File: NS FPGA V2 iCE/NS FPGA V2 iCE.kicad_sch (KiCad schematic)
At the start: 0 parts

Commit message: drew 30% of the schematic
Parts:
- added C1, C2, C3, C4, C5, C6, C7, C8: 10uF, symbol Device:C
- added C10, C11, C14: 0.1uF, symbol Device:C
- added C12, C13, C9: 4.7uF, symbol Device:C
- added D1: D_Schottky, symbol Device:D_Schottky
- added D2: LED, symbol Device:LED
- added J1: USB_C_Receptacle_USB2.0_14P, symbol Connector:USB_C_Receptacle_USB2.0_14P
- added R1: 1k, symbol Device:R
- added R2, R3: 5.1k, symbol Device:R
- added R4: 47.5k, symbol Device:R
- added R5: 22.1k, symbol Device:R
- added R6: 10k, symbol Device:R
- added U1: ICE40UP5K-SG48ITR, Package_DFN_QFN:QFN-48-1EP_7x7mm_P0.5mm_EP5.1x5.1mm, symbol FPGA_Lattice:ICE40UP5K-SG48ITR
- added U2: W25Q128JVS, Package_SO:SOIC-8_5.3x5.3mm_P1.27mm, symbol Memory_Flash:W25Q128JVS
- added U3: CP2102N-Axx-xQFN24, Package_DFN_QFN:QFN-24-1EP_4x4mm_P0.5mm_EP2.6x2.6mm, symbol Interface_USB:CP2102N-Axx-xQFN24
- added U4: AP2112K-3.3, Package_TO_SOT_SMD:SOT-23-5, symbol Regulator_Linear:AP2112K-3.3
- added U5: AP2112K-1.2, Package_TO_SOT_SMD:SOT-23-5, symbol Regulator_Linear:AP2112K-1.2
- added U6: AP2112K-2.5, Package_TO_SOT_SMD:SOT-23-5, symbol Regulator_Linear:AP2112K-2.5
- added U7: AP2112K-1.8, Package_TO_SOT_SMD:SOT-23-5, symbol Regulator_Linear:AP2112K-1.8
- added Y1: SG-210STF, Oscillator:Oscillator_SMD_SeikoEpson_SG210-4Pin_2.5x2.0mm, symbol Oscillator:SG-210STF
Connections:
- new net: C1.2, U4.1 (VIN), U4.3 (EN)
- new net: C4.2, U5.5 (VOUT)
- new net: J1.A5 (CC1), R2.1
- new net: J1.B5 (CC2), R3.1
- new net: C5.2, U6.1 (VIN), U6.3 (EN)
- new net: C2.2, U4.5 (VOUT)
- new net: C7.2, U7.1 (VIN), U7.3 (EN)
- new net: C3.2, U5.1 (VIN), U5.3 (EN)
- new net: C8.2, U7.5 (VOUT)
- new net: C13.1, C14.1, R6.2, U3.5 (VIO), U3.6 (VDD)
- new net: R4.1, R5.2, U3.8 (VBUS)
- new net: R6.1, U3.9 (~{RST})
- new net: U1.30 (VCC), U1.5 (VCC)
- new net: C6.2, U6.5 (VOUT)
- new net: D2.2 (A), R1.1
- new net +1V2: C4.1
- new net +1V8: C8.1
- new net +2V5: C6.1
- new net +3V3: C2.1, C3.1, C5.1, C7.1
- new net +5V: C1.1, C10.1, C9.1, D1.2 (A), J1.A4 (VBUS), J1.A9 (VBUS), J1.B4 (VBUS), J1.B9 (VBUS), R1.2, R5.1
- new net +5VP: C11.1, C12.1, D1.1 (K), U3.7 (VREGIN)
- new net D+: J1.A6 (D+), J1.B6 (D+), U3.3 (D+)
- new net D-: J1.A7 (D-), J1.B7 (D-), U3.4 (D-)
- new net GND: C10.2, C11.2, C12.2, C13.2, C14.2, C9.2, D2.1 (K), J1.A1 (GND), J1.A12 (GND), J1.B1 (GND), J1.B12 (GND), J1.S1 (SHIELD), R2.2, R3.2, R4.2, U3.2 (GND), U3.25 (GND), U4.2 (GND), U5.2 (GND), U6.2 (GND), U7.2 (GND)
- no-connect marks 0 -> 14
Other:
- note added: "NS iCE40UP FPGA"

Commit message: worked on the chip power delivery and power initialization timing
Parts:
- added C15, C17: 100nF, symbol Device:C
- added C16: 10uF, symbol Device:C
- added J2, J3: Conn_01x20_Pin, symbol Connector:Conn_01x20_Pin
- added R7: 10k, symbol Device:R
- added R8: 100, symbol Device:R
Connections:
- net +1V2: now also U1.30 (VCC), U1.5 (VCC), R8.2
- net +1V8: now also J2.5 (Pin_5)
- net +2V5: now also U1.24 (VPP_2V5), J2.4 (Pin_4)
- net +3V3: now also J2.3 (Pin_3)
- net +5V: now also J2.1 (Pin_1)
- net +5VP: now also U5.3 (EN), C15.2, R7.1
- net GND: now also U1.49 (GND), U2.4 (GND), Y1.2 (GND), C15.1, C16.2, C17.2, J2.2 (Pin_2)
- net at C1.2, U4.1 (VIN): no longer U4.3 (EN)
- net at C3.2, U5.1 (VIN): no longer U5.3 (EN)
- net at U1.29 (VCCPLL): now also C16.1, C17.1, R8.1
- new net: R7.2, U4.3 (EN)
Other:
- note added: "0603, 5%"

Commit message: added split differential voltage input selectors for each FPGA bank, wired up OSC and fixed vreg circuitry
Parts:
- added C18, C19: 0.1uF, symbol Device:C
- added D3: LED_ARGB, symbol Device:LED_ARGB
- added J4, J5: Conn_02x03_Odd_Even, symbol Connector_Generic:Conn_02x03_Odd_Even
- added J6: Conn_01x07_Pin, symbol Connector:Conn_01x07_Pin
- added R10, R11, R15: 10k, symbol Device:R
- added R12, R13, R14: 1.5k, symbol Device:R
- added R9: R22, symbol Device:R
- added SW1: SW_Push, symbol Switch:SW_Push
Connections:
- net +1V8: now also J4.2 (Pin_2), J5.2 (Pin_2)
- net +2V5: now also J4.4 (Pin_4), J5.4 (Pin_4)
- net +3V3: now also U1.22 (SPI_VCCIO1), U2.3 (~{WP}/IO_{2}), U2.7 (~{HOLD}/~{RESET}/IO_{3}), U2.8 (VCC), Y1.4 (Vcc), C18.2, C19.2, D3.1 (A), J4.6 (Pin_6), J5.6 (Pin_6), J6.1 (Pin_1), R10.1, R11.2
- net GND: now also C18.1, C19.1, J6.2 (Pin_2), SW1.2
- net SPI_SO: now reaches U1.14 (IOB_32a_SPI_SO)
- net SPI_SO: now also U2.2 (DO/IO_{1}), J6.5 (Pin_5)
- net SPI_SCK: now reaches U1.15 (IOB_34a_SPI_SCK)
- net SPI_SCK: now also U2.6 (CLK), J6.4 (Pin_4)
- net SPI_SS: now reaches U1.16 (IOB_35b_SPI_SS)
- net SPI_SS: now also U2.1 (~{CS}), J6.3 (Pin_3), R11.1
- net SPI_SI: now reaches U1.17 (IOB_33b_SPI_SI)
- net SPI_SI: now also U2.5 (DI/IO_{0}), J6.6 (Pin_6)
- net RXD: now reaches U1.18 (IOB_31b)
- net RXD: now also U3.20 (RXD)
- net FPGA_CLK: now reaches U1.20 (IOB_25b_G3)
- net FPGA_CLK: now also R9.2
- net TXD: now reaches U1.6 (IOB_13b)
- net TXD: now also U3.21 (TXD)
- net CRESET_B: now reaches U1.8 (~{CRESET})
- net CRESET_B: now also J6.7 (Pin_7)
- net at Y1.1 (~{ST}): now also R10.2
- net at Y1.3 (OUT): now also R9.1
- net at U1.33 (VCCIO_0): now also J4.1 (Pin_1), J4.3 (Pin_3), J4.5 (Pin_5), R15.2
- net at U1.39 (RGB0): now also R12.1
- net at U1.40 (RGB1): now also R13.1
- net at U1.41 (RGB2): now also R14.1
- net at U1.42 (IOT_51a): now also R15.1, SW1.1
- net at U1.1 (VCCIO_2): now also J5.1 (Pin_1), J5.3 (Pin_3), J5.5 (Pin_5)
- new net: D3.2 (RK), R12.2
- new net: D3.3 (GK), R13.2
- new net: D3.4 (BK), R14.2
- no-connect marks 14 -> 12
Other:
- moved on the sheet: J3

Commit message: completed drawing
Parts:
- added C20, C21, C22, C23, C24, C26: 0.1uF, symbol Device:C
- added C25: 1uF, symbol Device:C
- added D4: LED, symbol Device:LED
- added R16: 10k, symbol Device:R
- added R17: 1.5k, symbol Device:R
- added TP1, TP2, TP3, TP4: TestPoint_Small, symbol Connector:TestPoint_Small
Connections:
- net +1V2: now also C20.1, C24.1, C25.1, TP3.1
- net +1V8: now also TP4.1
- net +2V5: now also C26.2, TP2.1
- net +3V3: now also J2.18 (Pin_18), J3.18 (Pin_18), C21.1, TP1.1
- net +5V: now also J3.20 (Pin_20)
- net CRESET_B: now also R16.2; no longer U1.8 (~{CRESET})
- net GND: now also J2.10 (Pin_10), J2.19 (Pin_19), J3.10 (Pin_10), J3.19 (Pin_19), J3.2 (Pin_2), C20.2, C21.2, C22.2, C23.2, C24.2, C25.2, C26.1, R17.1
- net VCCIO_2: now reaches J5.1 (Pin_1), J5.3 (Pin_3), J5.5 (Pin_5), U1.1 (VCCIO_2)
- net VCCIO_2: now also C23.1
- net 1OB_18a: now reaches U1.10 (IOB_18a)
- net IOB_20a: now reaches U1.11 (IOB_20a)
- net IOB_22a: now reaches U1.12 (IOB_22a)
- net IOB_24a: now reaches U1.13 (IOB_24a)
- net IOB_29b: now reaches U1.19 (IOB_29b)
- net IOB_23b: now reaches U1.21 (IOB_23b)
- net at U1.7 (CDONE): now also D4.2 (A)
- net IOB_12a: now reaches U1.9 (IOB_16a)
- net IOT_37a: now reaches U1.23 (IOT_37a)
- net IOT_36b: now reaches U1.25 (IOT_36b)
- net IOT_39a: now reaches U1.26 (IOT_39a)
- net IOT_38b: now reaches U1.27 (IOT_38b)
- net IOT_41a: now reaches U1.28 (IOT_41a)
- net IOT_42b: now reaches U1.31 (IOT_42b)
- net IOT_43a: now reaches U1.32 (IOT_43a)
- net VCCIO_0: now reaches J4.1 (Pin_1), J4.3 (Pin_3), J4.5 (Pin_5), R15.2, U1.33 (VCCIO_0)
- net VCCIO_0: now also C22.1
- net IOT_44b: now reaches U1.34 (IOT_44b)
- net IOT_46b_G0: now reaches U1.35 (IOT_46b_G0)
- net IOT_48b: now reaches U1.36 (IOT_48b)
- net IOT_45a_G1: now reaches U1.37 (IOT_45a_G1)
- net IOT_50b: now reaches U1.38 (IOT_50b)
- net IOT_49a: now reaches U1.43 (IOT_49a)
- net IOB_6a: now reaches U1.2 (IOB_6a)
- net IOB_9b: now reaches U1.3 (IOB_9b)
- net IOB_8a: now reaches U1.4 (IOB_8a)
- net IOB_3b_G6: now reaches U1.44 (IOB_3b_G6)
- net IOB_5b: now reaches U1.45 (IOB_5b)
- net IOB_Oa: now reaches U1.46 (IOB_0a)
- net IOB_2a: now reaches U1.47 (IOB_2a)
- net IOB_4a: now reaches U1.48 (IOB_4a)
- new net: R16.1, U1.8 (~{CRESET})
- new net: D4.1 (K), R17.2
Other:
- moved on the sheet: C18, R10, R9, Y1

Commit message: assigned footprints
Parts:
- C1, C2, C3, C4, C5, C6, C7, C8: footprint (none) -> Capacitor_SMD:C_0603_1608Metric
- C10, C11, C12, C13, C14, C15, C16, C17, C18, C19, C20, C21, C22, C23, C24, C25, C26, C9: footprint (none) -> Capacitor_SMD:C_0402_1005Metric
- D1: footprint (none) -> Diode_SMD:D_0603_1608Metric
- D2, D4: footprint (none) -> LED_SMD:LED_0402_1005Metric
- D3: footprint (none) -> LED_SMD:LED_Cree-PLCC4_5x5mm_CW
- J1: footprint (none) -> Connector_USB:USB_C_Receptacle_HRO_TYPE-C-31-M-12
- J2, J3: footprint (none) -> Connector_PinHeader_2.54mm:PinHeader_1x20_P2.54mm_Vertical
- J4, J5: footprint (none) -> Connector_IDC:IDC-Header_2x03_P2.54mm_Vertical
- J6: footprint (none) -> Connector_PinHeader_2.54mm:PinHeader_1x07_P2.54mm_Vertical
- R1, R10, R11, R12, R13, R14, R15, R16, R17, R4, R5, R6, R7, R9: footprint (none) -> Resistor_SMD:R_0402_1005Metric
- R2, R3, R8: footprint (none) -> Resistor_SMD:R_0603_1608Metric
- SW1: footprint (none) -> Button_Switch_SMD:SW_Push_1P1T_NO_CK_KMR2
- TP1, TP2, TP3, TP4: footprint (none) -> TestPoint:TestPoint_Pad_D1.0mm
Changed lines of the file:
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@@
 			)
 		)
-		(property "Footprint" ""
+		(property "Footprint" "Capacitor_SMD:C_0402_1005Metric"
 			(at 145.7452 166.37 0)
 			(effects
@@
 			)
 		)
-		(property "Footprint" ""
+		(property "Footprint" "LED_SMD:LED_Cree-PLCC4_5x5mm_CW"
 			(at 90.17 101.6 0)
 			(effects
@@
 			)
 		)
-		(property "Footprint" ""
+		(property "Footprint" "Capacitor_SMD:C_0603_1608Metric"
 			(at 136.8552 224.79 0)
 			(effects
@@
 			)
 		)
-		(property "Footprint" ""
+		(property "Footprint" "Capacitor_SMD:C_0402_1005Metric"
 			(at 269.24 103.1748 0)
 			(effects
@@
 			)
 		)
-		(property "Footprint" ""
+		(property "Footprint" "Resistor_SMD:R_0402_1005Metric"
 			(at 74.93 133.858 90)
 			(effects
@@
 			)
 		)
-		(property "Footprint" ""
+		(property "Footprint" "Connector_IDC:IDC-Header_2x03_P2.54mm_Vertical"
 			(at 90.17 212.09 0)
 			(effects
@@
 			)
 		)
-		(property "Footprint" ""
+		(property "Footprint" "Capacitor_SMD:C_0402_1005Metric"
 			(at 171.1452 69.85 0)
 			(effects
@@
 			)
 		)
-		(property "Footprint" ""
+		(property "Footprint" "Resistor_SMD:R_0402_1005Metric"
 			(at 140.97 229.108 90)
 			(effects
@@
 			)
 		)
-		(property "Footprint" ""
+		(property "Footprint" "Resistor_SMD:R_0402_1005Metric"
 			(at 34.29 133.858 90)
 			(effects
@@
 			)
 		)
-		(property "Footprint" ""
+		(property "Footprint" "Capacitor_SMD:C_0603_1608Metric"
 			(at 225.7552 224.79 0)
 			(effects
@@
 			)
 		)
-		(property "Footprint" ""
+		(property "Footprint" "Connector_USB:USB_C_Receptacle_HRO_TYPE-C-31-M-12"
 			(at 354.33 95.25 0)
 			(effects
@@
 			)
 		)
-		(property "Footprint" ""
+		(property "Footprint" "Capacitor_SMD:C_0603_1608Metric"
 			(at 136.8552 254 0)
 			(effects
@@
 			)
 		)
-		(property "Footprint" ""
+		(property "Footprint" "Capacitor_SMD:C_0603_1608Metric"
 			(at 167.3352 224.79 0)
 			(effects
@@
 			)
 		)
-		(property "Footprint" ""
+		(property "Footprint" "Capacitor_SMD:C_0603_1608Metric"
 			(at 194.0052 254 0)
 			(effects
@@
 			)
 		)
-		(property "Footprint" ""
+		(property "Footprint" "Capacitor_SMD:C_0603_1608Metric"
 			(at 224.4852 254 0)
 			(effects
@@
 			)
 		)
-		(property "Footprint" ""
+		(property "Footprint" "Capacitor_SMD:C_0402_1005Metric"
 			(at 387.35 67.6148 0)
 			(effects
@@
 			)
 		)
-		(property "Footprint" ""
+		(property "Footprint" "Connector_PinHeader_2.54mm:PinHeader_1x20_P2.54mm_Vertical"
 			(at 344.17 205.74 0)
 			(effects
@@
 			)
 		)
-		(property "Footprint" ""
+		(property "Footprint" "Resistor_SMD:R_0603_1608Metric"
 			(at 372.11 89.408 90)
 			(effects
@@
 			)
 		)
-		(property "Footprint" ""
+		(property "Footprint" "Button_Switch_SMD:SW_Push_1P1T_NO_CK_KMR2"
 			(at 90.17 72.39 0)
 			(effects
@@
 			)
 		)
-		(property "Footprint" ""
+		(property "Footprint" "Capacitor_SMD:C_0402_1005Metric"
 			(at 136.1948 227.33 0)
 			(effects
@@
 			)
 		)
-		(property "Footprint" ""
+		(property "Footprint" "Resistor_SMD:R_0402_1005Metric"
 			(at 81.28 97.028 90)
 			(effects
@@
 			)
 		)
-		(property "Footprint" ""
+		(property "Footprint" "TestPoint:TestPoint_Pad_D1.0mm"
 			(at 175.26 215.9 0)
 			(effects
@@
 			)
 		)
-		(property "Footprint" ""
+		(property "Footprint" "Resistor_SMD:R_0402_1005Metric"
 			(at 172.72 124.968 90)
 			(effects
@@
 			)
 		)
-		(property "Footprint" ""
+		(property "Footprint" "Capacitor_SMD:C_0402_1005Metric"
 			(at 129.2352 166.37 0)
 			(effects
@@
 			)
 		)
-		(property "Footprint" ""
+		(property "Footprint" "Capacitor_SMD:C_0603_1608Metric"
 			(at 167.3352 254 0)
 			(effects
@@
 			)
 		)
-		(property "Footprint" ""
+		(property "Footprint" "Capacitor_SMD:C_0402_1005Metric"
 			(at 387.35 73.9648 0)
 			(effects
@@
 			)
 		)
-		(property "Footprint" ""
+		(property "Footprint" "TestPoint:TestPoint_Pad_D1.0mm"
 			(at 237.49 214.63 0)
 			(effects
@@
 			)
 		)
-		(property "Footprint" ""
+		(property "Footprint" "Capacitor_SMD:C_0402_1005Metric"
 			(at 177.4952 166.37 0)
 			(effects
@@
 			)
 		)
-		(property "Footprint" ""
+		(property "Footprint" "Capacitor_SMD:C_0402_1005Metric"
 			(at 161.29 48.5648 0)
 			(effects
@@
 			)
 		)
-		(property "Footprint" ""
+		(property "Footprint" "Capacitor_SMD:C_0603_1608Metric"
 			(at 194.0052 224.79 0)
 			(effects
@@
 			)
 		)
-		(property "Footprint" ""
+		(property "Footprint" "Diode_SMD:D_0603_1608Metric"
 			(at 386.08 48.26 0)
 			(effects
@@
 			)
 		)
-		(property "Footprint" ""
+		(property "Footprint" "TestPoint:TestPoint_Pad_D1.0mm"
 			(at 240.03 245.11 0)
 			(effects
@@
 			)
 		)
-		(property "Footprint" ""
+		(property "Footprint" "Resistor_SMD:R_0402_1005Metric"
 			(at 195.58 124.968 90)
 			(effects
@@
 			)
 		)
-		(property "Footprint" ""
+		(property "Footprint" "Capacitor_SMD:C_0402_1005Metric"
 			(at 181.3052 69.85 0)
 			(effects
@@
 			)
 		)
-		(property "Footprint" ""
+		(property "Footprint" "LED_SMD:LED_0402_1005Metric"
 			(at 356.87 43.18 0)
 			(effects
@@
 			)
 		)
-		(property "Footprint" ""
+		(property "Footprint" "Capacitor_SMD:C_0402_1005Metric"
 			(at 187.96 112.7252 0)
 			(effects
@@
 			)
 		)
-		(property "Footprint" ""
+		(property "Footprint" "Connector_PinHeader_2.54mm:PinHeader_1x20_P2.54mm_Vertical"
 			(at 373.38 205.74 0)
 			(effects
@@
 			)
 		)
-		(property "Footprint" ""
+		(property "Footprint" "Capacitor_SMD:C_0402_1005Metric"
 			(at 161.29 42.2148 0)
 			(effects
@@
 			)
 		)
-		(property "Footprint" ""
+		(property "Footprint" "Resistor_SMD:R_0603_1608Metric"
 			(at 185.42 64.008 90)
 			(effects
@@
 			)
 		)
-		(property "Footprint" ""
+		(property "Footprint" "Capacitor_SMD:C_0402_1005Metric"
 			(at 245.11 108.9152 0)
 			(effects
@@
 			)
 		)
-		(property "Footprint" ""
+		(property "Footprint" "Resistor_SMD:R_0603_1608Metric"
 			(at 372.11 86.868 90)
 			(effects
@@
 			)
 		)
-		(property "Footprint" ""
+		(property "Footprint" "Resistor_SMD:R_0402_1005Metric"
 			(at 275.59 122.428 90)
 			(effects
@@
 			)
 		)
-		(property "Footprint" ""
+		(property "Footprint" "Capacitor_SMD:C_0402_1005Metric"
 			(at 245.11 101.2952 0)
 			(effects
@@
 			)
 		)
-		(property "Footprint" ""
+		(property "Footprint" "Capacitor_SMD:C_0402_1005Metric"
 			(at 147.32 66.3448 0)
 			(effects
@@
 			)
 		)
-		(property "Footprint" ""
+		(property "Footprint" "Resistor_SMD:R_0402_1005Metric"
 			(at 295.402 128.27 90)
 			(effects
@@
 			)
 		)
-		(property "Footprint" ""
+		(property "Footprint" "Resistor_SMD:R_0402_1005Metric"
 			(at 81.28 102.108 90)
 			(effects
@@
 			)
 		)
-		(property "Footprint" ""
+		(property "Footprint" "Resistor_SMD:R_0402_1005Metric"
 			(at 246.888 44.45 90)
 			(effects
@@
 			)
 		)
-		(property "Footprint" ""
+		(property "Footprint" "Resistor_SMD:R_0402_1005Metric"
 			(at 66.04 40.132 90)
 			(effects
@@
 			)
 		)
-		(property "Footprint" ""
+		(property "Footprint" "Resistor_SMD:R_0402_1005Metric"
 			(at 81.28 107.188 90)
 			(effects
@@
 			)
 		)
-		(property "Footprint" ""
+		(property "Footprint" "Resistor_SMD:R_0402_1005Metric"
 			(at 295.402 137.16 90)
 			(effects
@@
 			)
 		)
-		(property "Footprint" ""
+		(property "Footprint" "Connector_PinHeader_2.54mm:PinHeader_1x07_P2.54mm_Vertical"
 			(at 359.41 234.95 0)
 			(effects
@@
 			)
 		)
-		(property "Footprint" ""
+		(property "Footprint" "Capacitor_SMD:C_0402_1005Metric"
 			(at 262.89 44.1452 0)
 			(effects
@@
 			)
 		)
-		(property "Footprint" ""
+		(property "Footprint" "TestPoint:TestPoint_Pad_D1.0mm"
 			(at 176.53 243.84 0)
 			(effects
@@
 			)
 		)
-		(property "Footprint" ""
+		(property "Footprint" "Resistor_SMD:R_0402_1005Metric"
 			(at 367.03 44.958 90)
 			(effects
@@
 			)
 		)
-		(property "Footprint" ""
+		(property "Footprint" "Connector_IDC:IDC-Header_2x03_P2.54mm_Vertical"
 			(at 93.98 36.83 0)
 			(effects
@@
 			)
 		)
-		(property "Footprint" ""
+		(property "Footprint" "Capacitor_SMD:C_0402_1005Metric"
 			(at 160.9852 166.37 0)
 			(effects
@@
 			)
 		)
-		(property "Footprint" ""
+		(property "Footprint" "LED_SMD:LED_0402_1005Metric"
 			(at 41.91 132.08 0)
 			(effects
@@
 			)
 		)
-		(property "Footprint" ""
+		(property "Footprint" "Capacitor_SMD:C_0402_1005Metric"
 			(at 269.24 110.7948 0)
 			(effects

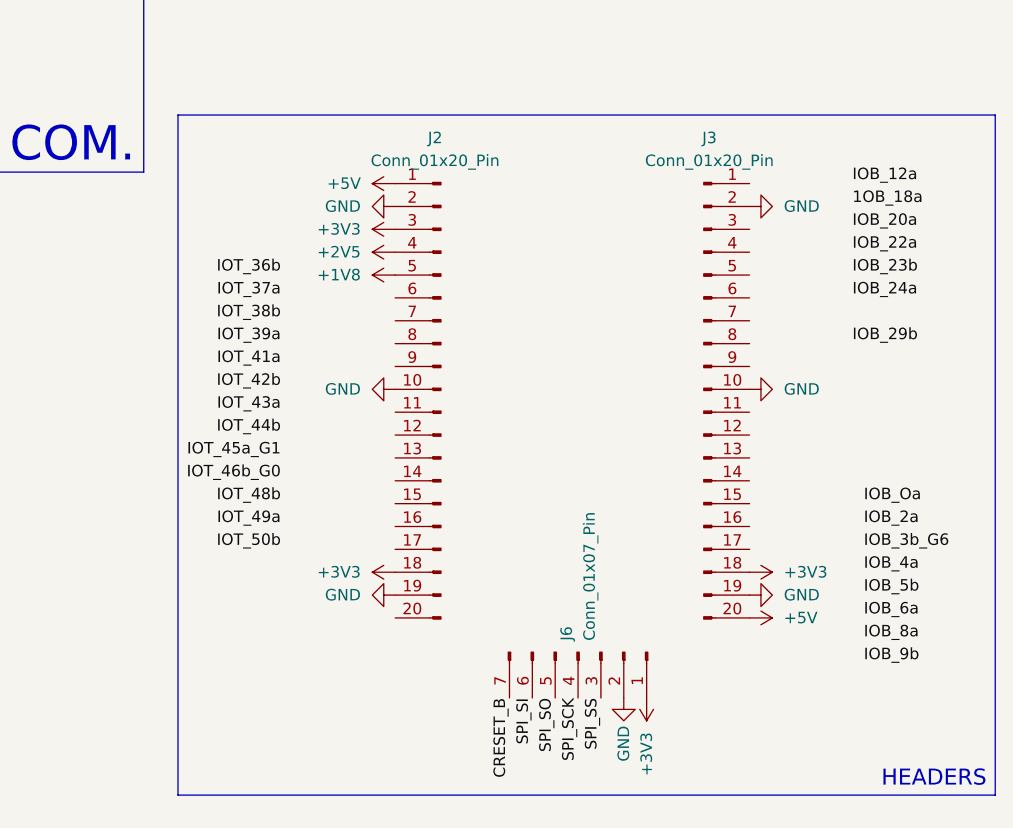
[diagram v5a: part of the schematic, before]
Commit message: Completed Placement, Routing and Partial Silkscreen
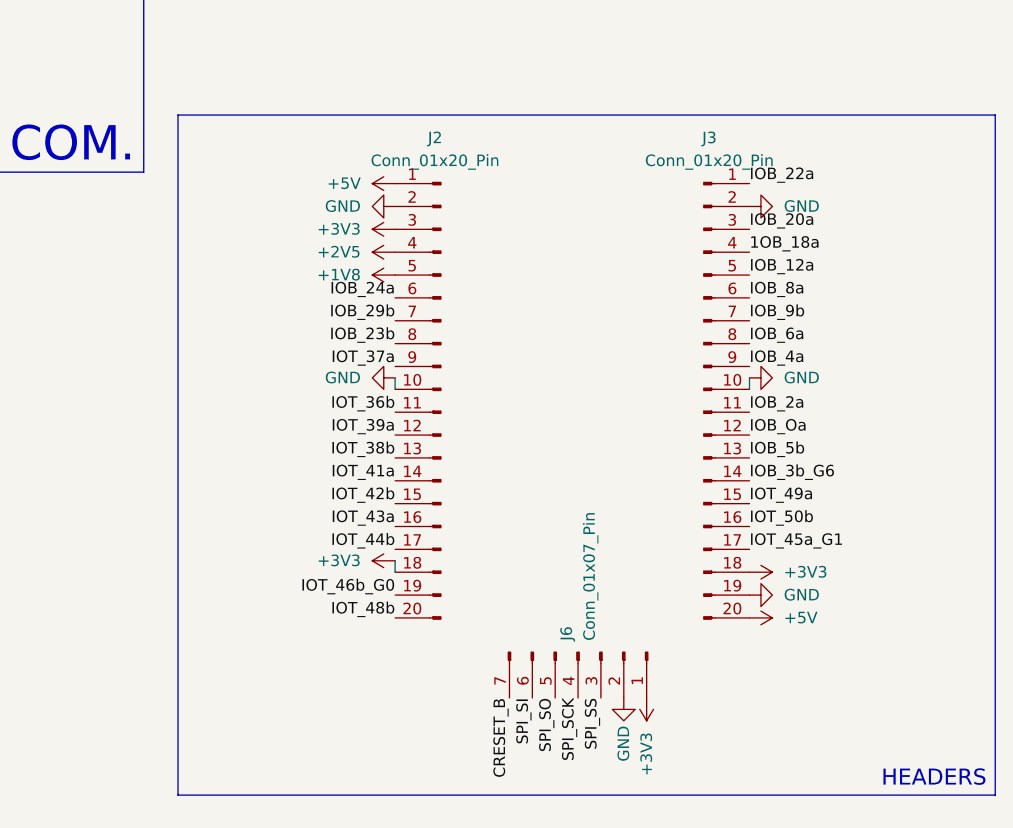
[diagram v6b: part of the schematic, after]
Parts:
- J4, J5: footprint Connector_IDC:IDC-Header_2x03_P2.54mm_Vertical -> Connector_PinHeader_1.00mm:PinHeader_2x03_P1.00mm_Vertical
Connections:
- net 1OB_18a: now also J3.4 (Pin_4)
- net GND: no longer J2.19 (Pin_19)
- net IOB_12a: now also J3.5 (Pin_5)
- net IOB_20a: now also J3.3 (Pin_3)
- net IOB_22a: now also J3.1 (Pin_1)
- net IOB_23b: now also J2.8 (Pin_8)
- net IOB_24a: now also J2.6 (Pin_6)
- net IOB_29b: now also J2.7 (Pin_7)
- net IOB_2a: now also J3.11 (Pin_11)
- net IOB_3b_G6: now also J3.14 (Pin_14)
- net IOB_4a: now also J3.9 (Pin_9)
- net IOB_5b: now also J3.13 (Pin_13)
- net IOB_6a: now also J3.8 (Pin_8)
- net IOB_8a: now also J3.6 (Pin_6)
- net IOB_9b: now also J3.7 (Pin_7)
- net IOB_Oa: now also J3.12 (Pin_12)
- net IOT_36b: now also J2.11 (Pin_11)
- net IOT_37a: now also J2.9 (Pin_9)
- net IOT_38b: now also J2.13 (Pin_13)
- net IOT_39a: now also J2.12 (Pin_12)
- net IOT_41a: now also J2.14 (Pin_14)
- net IOT_42b: now also J2.15 (Pin_15)
- net IOT_43a: now also J2.16 (Pin_16)
- net IOT_44b: now also J2.17 (Pin_17)
- net IOT_45a_G1: now also J3.17 (Pin_17)
- net IOT_46b_G0: now also J2.19 (Pin_19)
- net IOT_48b: now also J2.20 (Pin_20)
- net IOT_49a: now also J3.15 (Pin_15)
- net IOT_50b: now also J3.16 (Pin_16)

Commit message: done with BOM/CPL
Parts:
- D3: footprint LED_SMD:LED_Cree-PLCC4_5x5mm_CW -> LED_SMD:LED_RGB_Wuerth-PLCC4_3.2x2.8mm_150141M173100
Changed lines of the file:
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@@
 			)
 		)
-		(property "Footprint" "LED_SMD:LED_Cree-PLCC4_5x5mm_CW"
+		(property "Footprint" "LED_SMD:LED_RGB_Wuerth-PLCC4_3.2x2.8mm_150141M173100"
 			(at 90.17 101.6 0)
 			(effects
